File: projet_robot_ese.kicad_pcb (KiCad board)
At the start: 4 copper layers, 140 x 40 mm, 89 parts, among them J201 Conn_01x02, J202 Conn_01x04, J203 Conn_01x04, J204 Conn_01x04, J301 Conn_01x06, J302 Conn_01x06, J401 Conn_02x07_Odd_Even, J402 Conn_01x02, J403 Conn_01x02, J404 Conn_01x07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

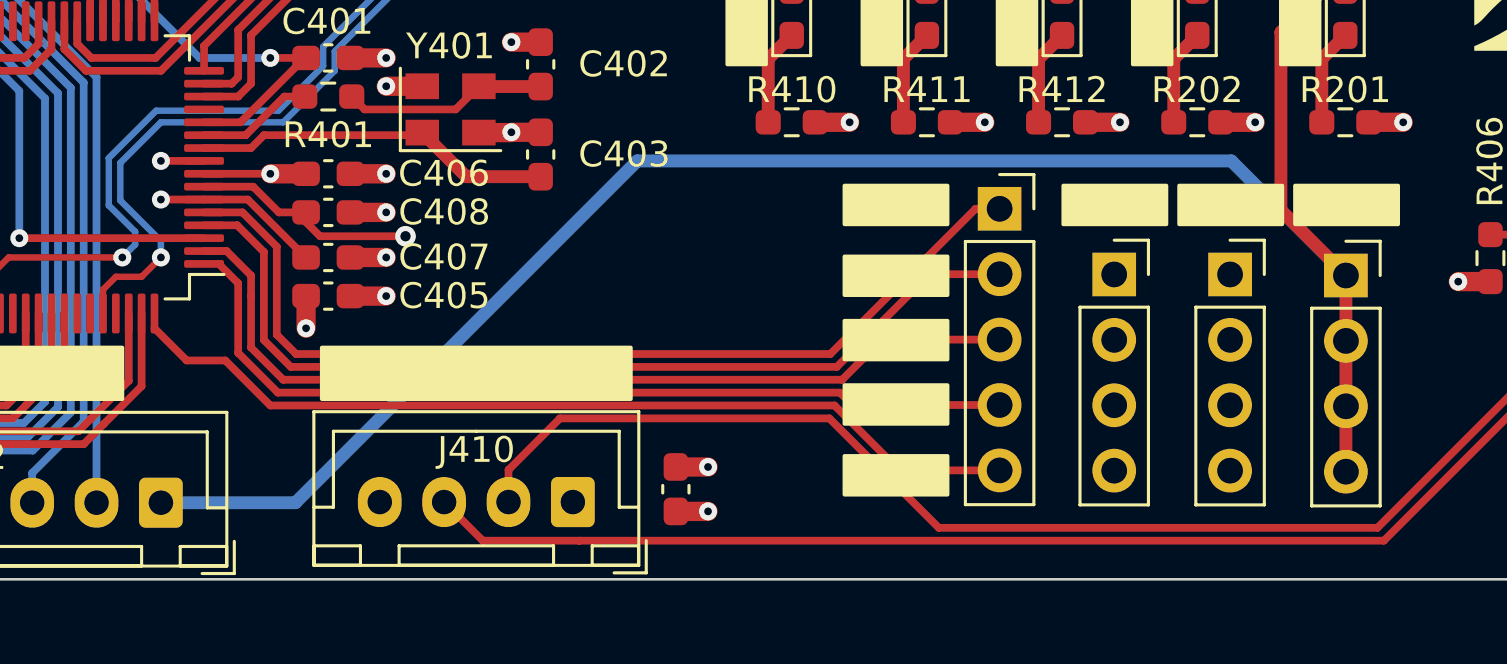
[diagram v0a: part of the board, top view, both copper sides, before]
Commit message: Color sensor modif
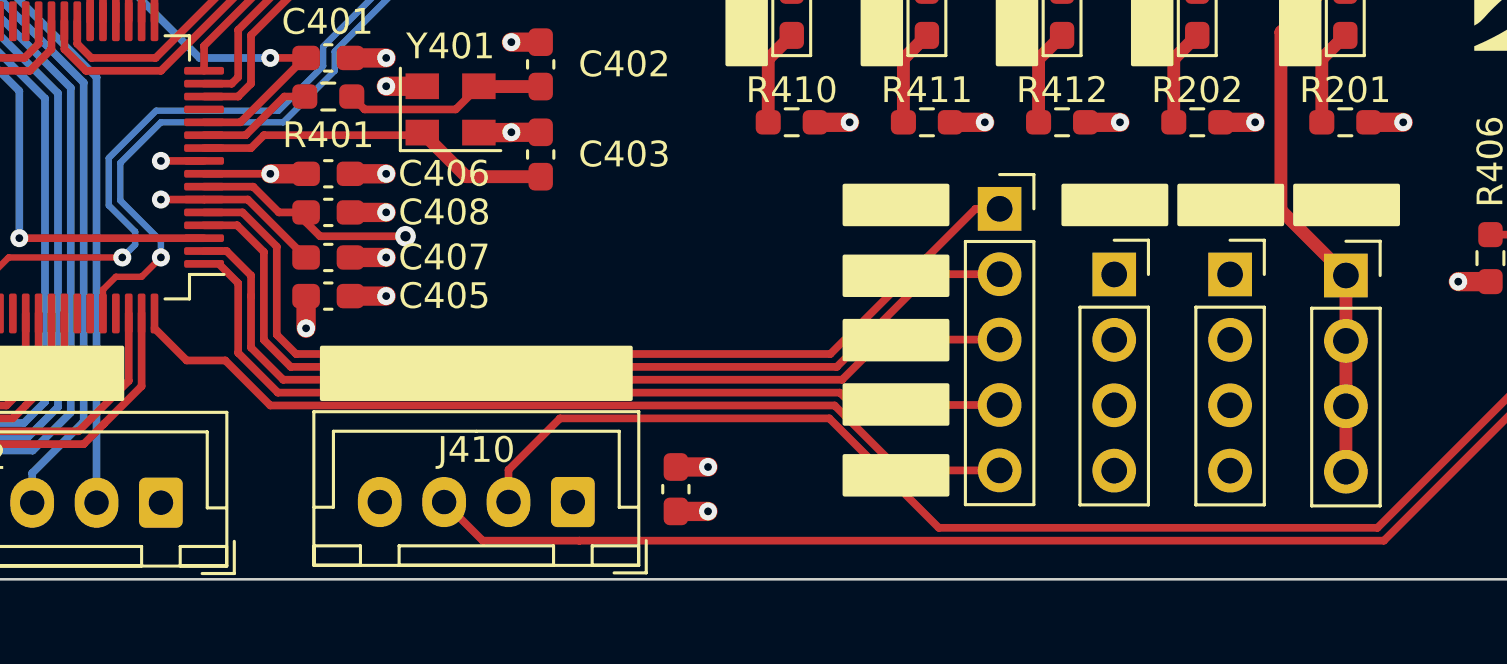
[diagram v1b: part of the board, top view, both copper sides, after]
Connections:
- C204 pad 1: VREF -> UP_VBAT
- C405 pad 1: VREF -> UP_VBAT
- C406 pad 1: VREF -> UP_VBAT
- C407 pad 1: VREF -> UP_VBAT
- C408 pad 1: VREF -> UP_VBAT
- C410 pad 1: VREF -> UP_VBAT
- D203 pad 2: VREF -> UP_VBAT
- J203 pad 1: VREF -> UP_VBAT
- J203 pad 2: VREF -> UP_VBAT
- J203 pad 3: VREF -> UP_VBAT
- J203 pad 4: VREF -> UP_VBAT
- J401 pad 3: VREF -> UP_VBAT
- J404 pad 2: VREF -> UP_VBAT
- J406 pad 2: VREF -> UP_VBAT
- J410 pad 1: VREF -> UP_VBAT
- J412 pad 1: +5V -> UP_VBAT
- R403 pad 1: VREF -> UP_VBAT
- R405 pad 1: VREF -> UP_VBAT
- R406 pad 1: VREF -> UP_VBAT
- R407 pad 1: VREF -> UP_VBAT
- R408 pad 1: VREF -> UP_VBAT
- R409 pad 1: VREF -> UP_VBAT
- R413 pad 2: VREF -> UP_VBAT
- R414 pad 2: VREF -> UP_VBAT
- U202 pad 5: VREF -> UP_VBAT
- U401 pad 6: VREF -> UP_VBAT
- U401 pad 7: VREF -> UP_VBAT
- U401 pad 8: VREF -> UP_VBAT
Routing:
- net VREF: track 40.2 -> 0.00 mm, vias 17 -> 0
- net UP_VBAT: track 0.00 -> 40.2 mm, vias 0 -> 17
- net +5V: track 250.9 -> 244.9 mm
- added copper zone on In2.Cu, net UP_VBAT
- removed copper zone on In2.Cu, net VREF
